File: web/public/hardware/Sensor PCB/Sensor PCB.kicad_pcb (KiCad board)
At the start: 2 copper layers, 65 x 60 mm, 20 parts, among them J1 Conn_01x08_Pin, J2 Conn_01x08_Pin, J3 Conn_01x06_Pin, J4 Conn_01x06_Pin, U1 DRV5033AJxDBZ, U2 DRV5033AJxDBZ, U3 DRV5033AJxDBZ, U4 DRV5033AJxDBZ, U5 74LS11, U6 74LS11

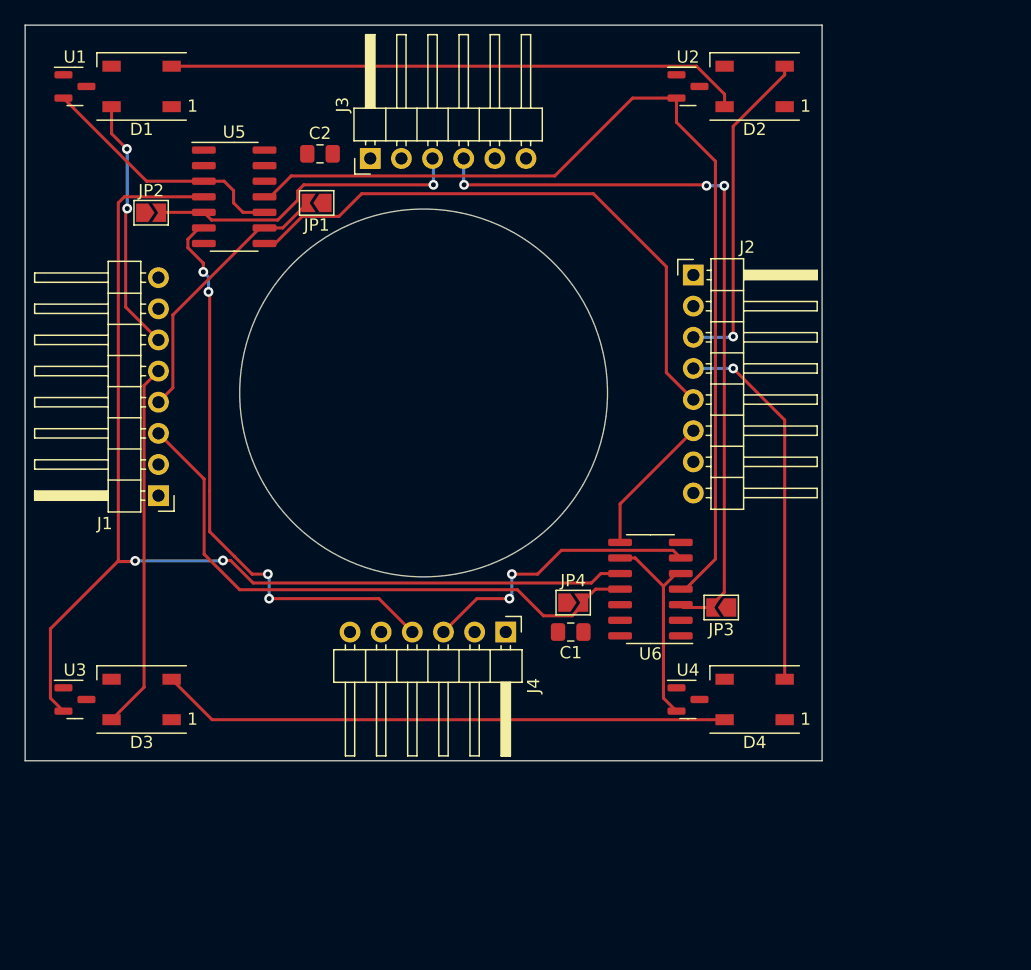
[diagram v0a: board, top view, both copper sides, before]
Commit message: Route PCB power and change sch/PCB page size to US letter
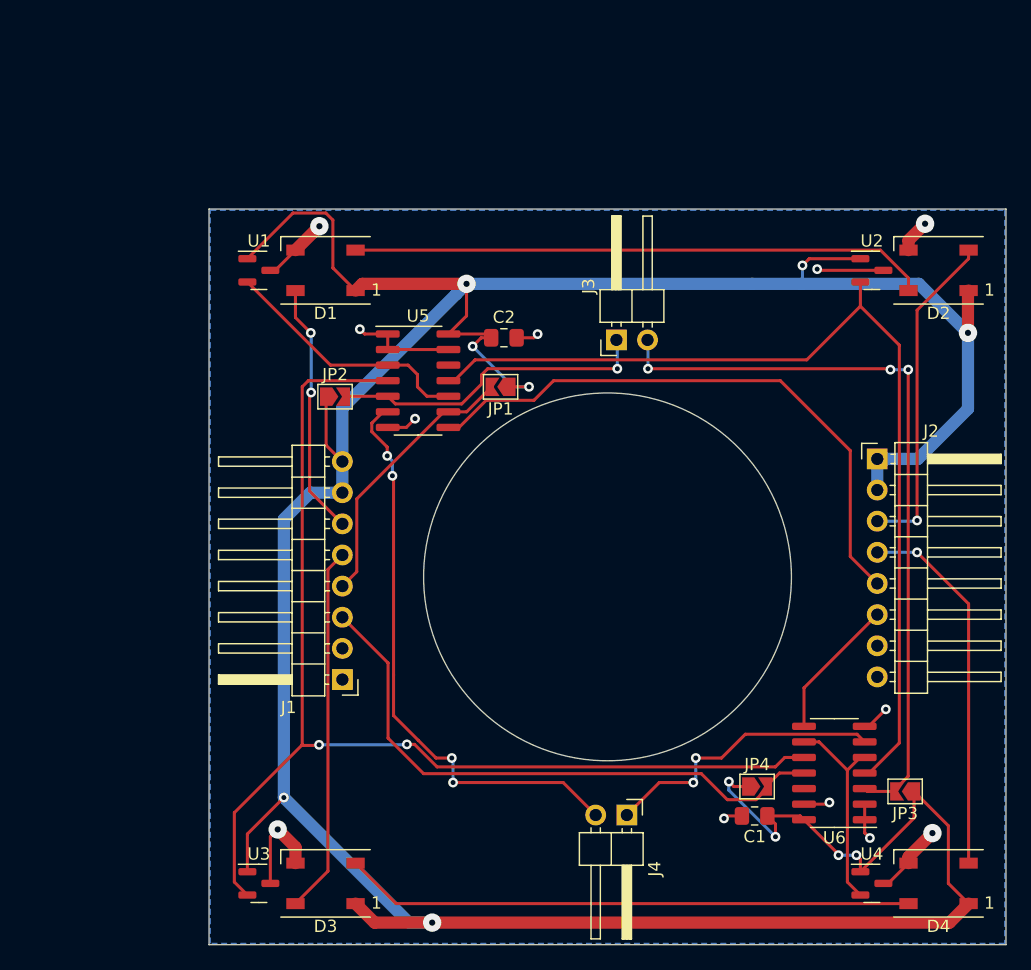
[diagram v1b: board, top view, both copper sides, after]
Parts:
- J3, J4: value Conn_01x06_Pin -> Conn_01x02_Pin; footprint Connector_PinHeader_2.54mm:PinHeader_1x06_P2.54mm_Horizontal -> Connector_PinHeader_2.54mm:PinHeader_1x02_P2.54mm_Horizontal
- moved J3 24.9 mm to (143.2, 70.7)
- moved C2 21.2 mm to (134.1, 70.5)
- moved C1 21.2 mm to (154.5, 109.5)
- moved D1 21.2 mm to (119.5, 65.0)
- moved D2 21.2 mm to (169.5, 65.0)
- moved D3 21.2 mm to (119.5, 115.0)
- moved D4 21.2 mm to (169.5, 115.0)
- moved J1 21.2 mm to (120.9, 98.4)
- moved J2 21.2 mm to (164.5, 80.4)
- moved JP1 21.2 mm to (133.8, 74.5)
- moved JP2 21.2 mm to (120.3, 75.3)
- moved JP3 21.2 mm to (166.8, 107.5)
- moved JP4 21.2 mm to (154.7, 107.1)
- moved U1 21.2 mm to (114.1, 65.0)
- moved U2 21.2 mm to (164.1, 65.0)
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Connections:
- J3 pad 1: +5V -> /COL1_IN
- J3 pad 2: +5V -> /COL2_IN
- J4 pad 1: GND -> /COL2_OUT
- J4 pad 2: GND -> /COL1_OUT
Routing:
- net +5V: track 0.00 -> 282.2 mm, vias 0 -> 11
- net GND: track 0.00 -> 49.6 mm, vias 0 -> 12
- net Net-(U2-OUT): track 79.7 -> 78.9 mm
- added copper zone on B.Cu, net GND

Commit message: Update production files
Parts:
- added H1: MountingHole, MountingHole:MountingHole_2.7mm_M2.5, F.Cu at (130.0, 112.1)
- added H2: MountingHole, MountingHole:MountingHole_2.7mm_M2.5, F.Cu at (113.9, 73.1)
- added H3: MountingHole, MountingHole:MountingHole_2.7mm_M2.5, F.Cu at (159.6, 77.2)
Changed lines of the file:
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@@
   (net 21 "unconnected-(U5-Pad12)")
   (net 22 "unconnected-(U6-Pad12)")
+  (footprint "MountingHole:MountingHole_2.7mm_M2.5" (layer "F.Cu")
+    (at 159.6 77.2)
+    (descr "Mounting Hole 2.7mm, no annular, M2.5")
+    (tags "mounting hole 2.7mm no annular m2.5")
+    (property "Sheetfile" "Sensor PCB.kicad_sch")
+    (property "Sheetname" "")
+    (property "ki_description" "Mounting Hole without connection")
+    (property "ki_keywords" "mounting hole")
+    (attr exclude_from_pos_files)
+    (fp_text reference "H3" (at 0 -3.7) (layer "F.SilkS")
+        (effects (font (size 1 1) (thickness 0.15)))
+    )
+    (fp_text value "MountingHole" (at 0 3.7) (layer "F.Fab")
+        (effects (font (size 1 1) (thickness 0.15)))
+    )
+    (fp_text user "${REFERENCE}" (at 0 0) (layer "F.Fab")
+        (effects (font (size 1 1) (thickness 0.15)))
+    )
+    (fp_circle (center 0 0) (end 2.7 0)
+      (stroke (width 0.15) (type solid)) (fill none) (layer "Cmts.User"))
+    (fp_circle (center 0 0) (end 2.95 0)
+      (stroke (width 0.05) (type solid)) (fill none) (layer "F.CrtYd"))
+    (pad "" np_thru_hole circle (at 0 0) (size 2.7 2.7) (drill 2.7) (layers "*.Cu" "*.Mask"))
+  )
+  (footprint "MountingHole:MountingHole_2.7mm_M2.5" (layer "F.Cu")
+    (at 113.9 73.1)
+    (descr "Mounting Hole 2.7mm, no annular, M2.5")
+    (tags "mounting hole 2.7mm no annular m2.5")
+    (property "Sheetfile" "Sensor PCB.kicad_sch")
+    (property "Sheetname" "")
+    (property "ki_description" "Mounting Hole without connection")
+    (property "ki_keywords" "mounting hole")
+    (attr exclude_from_pos_files)
+    (fp_text reference "H2" (at 0 -3.7) (layer "F.SilkS")
+        (effects (font (size 1 1) (thickness 0.15)))
+    )
+    (fp_text value "MountingHole" (at 0 3.7) (layer "F.Fab")
+        (effects (font (size 1 1) (thickness 0.15)))
+    )
+    (fp_text user "${REFERENCE}" (at 0 0) (layer "F.Fab")
+        (effects (font (size 1 1) (thickness 0.15)))
+    )
+    (fp_circle (center 0 0) (end 2.7 0)
+      (stroke (width 0.15) (type solid)) (fill none) (layer "Cmts.User"))
+    (fp_circle (center 0 0) (end 2.95 0)
+      (stroke (width 0.05) (type solid)) (fill none) (layer "F.CrtYd"))
+    (pad "" np_thru_hole circle (at 0 0) (size 2.7 2.7) (drill 2.7) (layers "*.Cu" "*.Mask"))
+  )
   (footprint "LED_SMD:LED_WS2812B_PLCC4_5.0x5.0mm_P3.2mm" (layer "F.Cu")
     (at 169.5 115 180)
@@
     (fp_line (start 1 0.625) (end -1 0.625)
       (stroke (width 0.1) (type solid)) (layer "F.Fab"))
-    (pad "1" smd roundrect (at -1.0375 0) (size 1.175 1.45) (layers "F.Cu" "F.Paste" "F.Mask") (roundrect_rratio 0.212766)
+    (pad "1" smd roundrect (at -1.0375 0) (size 1.175 1.45) (layers "F.Cu" "F.Paste" "F.Mask") (roundrect_rratio 0.2127659574)
       (net 1 "+5V") (pintype "passive"))
-    (pad "2" smd roundrect (at 1.0375 0) (size 1.175 1.45) (layers "F.Cu" "F.Paste" "F.Mask") (roundrect_rratio 0.212766)
+    (pad "2" smd roundrect (at 1.0375 0) (size 1.175 1.45) (layers "F.Cu" "F.Paste" "F.Mask") (roundrect_rratio 0.2127659574)
       (net 2 "GND") (pintype "passive"))
     (model "${KICAD6_3DMODEL_DIR}/Capacitor_SMD.3dshapes/C_0805_2012Metric.wrl"
@@
     )
   )
+  (footprint "MountingHole:MountingHole_2.7mm_M2.5" (layer "F.Cu")
+    (at 130 112.1)
+    (descr "Mounting Hole 2.7mm, no annular, M2.5")
+    (tags "mounting hole 2.7mm no annular m2.5")
+    (property "Sheetfile" "Sensor PCB.kicad_sch")
+    (property "Sheetname" "")
+    (property "ki_description" "Mounting Hole without connection")
+    (property "ki_keywords" "mounting hole")
+    (attr exclude_from_pos_files)
+    (fp_text reference "H1" (at 0 -3.7) (layer "F.SilkS")
+        (effects (font (size 1 1) (thickness 0.15)))
+    )
+    (fp_text value "MountingHole" (at 0 3.7) (layer "F.Fab")
+        (effects (font (size 1 1) (thickness 0.15)))
+    )
+    (fp_text user "${REFERENCE}" (at 0 0) (layer "F.Fab")
+        (effects (font (size 1 1) (thickness 0.15)))
+    )
+    (fp_circle (center 0 0) (end 2.7 0)
+      (stroke (width 0.15) (type solid)) (fill none) (layer "Cmts.User"))
+    (fp_circle (center 0 0) (end 2.95 0)
+      (stroke (width 0.05) (type solid)) (fill none) (layer "F.CrtYd"))
+    (pad "" np_thru_hole circle (at 0 0) (size 2.7 2.7) (drill 2.7) (layers "*.Cu" "*.Mask"))
+  )
   (footprint "Jumper:SolderJumper-2_P1.3mm_Open_TrianglePad1.0x1.5mm" (layer "F.Cu")
     (at 154.7 107.1)
@@
     (fp_line (start 1 0.625) (end -1 0.625)
       (stroke (width 0.1) (type solid)) (layer "F.Fab"))
-    (pad "1" smd roundrect (at -1.0375 0 180) (size 1.175 1.45) (layers "F.Cu" "F.Paste" "F.Mask") (roundrect_rratio 0.212766)
+    (pad "1" smd roundrect (at -1.0375 0 180) (size 1.175 1.45) (layers "F.Cu" "F.Paste" "F.Mask") (roundrect_rratio 0.2127659574)
       (net 1 "+5V") (pintype "passive"))
-    (pad "2" smd roundrect (at 1.0375 0 180) (size 1.175 1.45) (layers "F.Cu" "F.Paste" "F.Mask") (roundrect_rratio 0.212766)
+    (pad "2" smd roundrect (at 1.0375 0 180) (size 1.175 1.45) (layers "F.Cu" "F.Paste" "F.Mask") (roundrect_rratio 0.2127659574)
       (net 2 "GND") (pintype "passive"))
     (model "${KICAD6_3DMODEL_DIR}/Capacitor_SMD.3dshapes/C_0805_2012Metric.wrl"
@@
   (segment (start 154.60962 108.175) (end 155.425 107.35962) (width 0.25) (layer "F.Cu") (net 10))
   (segment (start 127.5 106.05) (end 150.15 106.05) (width 0.25) (layer "F.Cu") (net 10))
-  (segment (start 156.6 74) (end 162.3 79.7) (width 0.25) (layer "F.Cu") (net 11))
-  (segment (start 138.1 74) (end 156.6 74) (width 0.25) (layer "F.Cu") (net 11))
   (segment (start 129.525 77.81) (end 130.39 77.81) (width 0.25) (layer "F.Cu") (net 11))
-  (segment (start 162.3 79.7) (end 162.3 88.34) (width 0.25) (layer "F.Cu") (net 11))
+  (segment (start 132.6 75.6) (end 136.5 75.6) (width 0.25) (layer "F.Cu") (net 11))
+  (segment (start 155 79.3) (end 156.9 81.2) (width 0.25) (layer "F.Cu") (net 11))
+  (segment (start 161.1 81.2) (end 162.3 82.4) (width 0.25) (layer "F.Cu") (net 11))
+  (segment (start 138.1 74) (end 152.3 74) (width 0.25) (layer "F.Cu") (net 11))
+  (segment (start 155 76.7) (end 155 79.3) (width 0.25) (layer "F.Cu") (net 11))
+  (segment (start 130.39 77.81) (end 132.6 75.6) (width 0.25) (layer "F.Cu") (net 11))
+  (segment (start 162.3 82.4) (end 162.3 88.34) (width 0.25) (layer "F.Cu") (net 11))
+  (segment (start 156.9 81.2) (end 161.1 81.2) (width 0.25) (layer "F.Cu") (net 11))
   (segment (start 136.5 75.6) (end 138.1 74) (width 0.25) (layer "F.Cu") (net 11))
-  (segment (start 130.39 77.81) (end 132.6 75.6) (width 0.25) (layer "F.Cu") (net 11))
-  (segment (start 132.6 75.6) (end 136.5 75.6) (width 0.25) (layer "F.Cu") (net 11))
   (segment (start 162.3 88.34) (end 164.5 90.54) (width 0.25) (layer "F.Cu") (net 11))
+  (segment (start 152.3 74) (end 155 76.7) (width 0.25) (layer "F.Cu") (net 11))
   (segment (start 158.525 102.19) (end 158.525 99.055) (width 0.25) (layer "F.Cu") (net 12))
   (segment (start 158.525 99.055) (end 164.5 93.08) (width 0.25) (layer "F.Cu") (net 12))

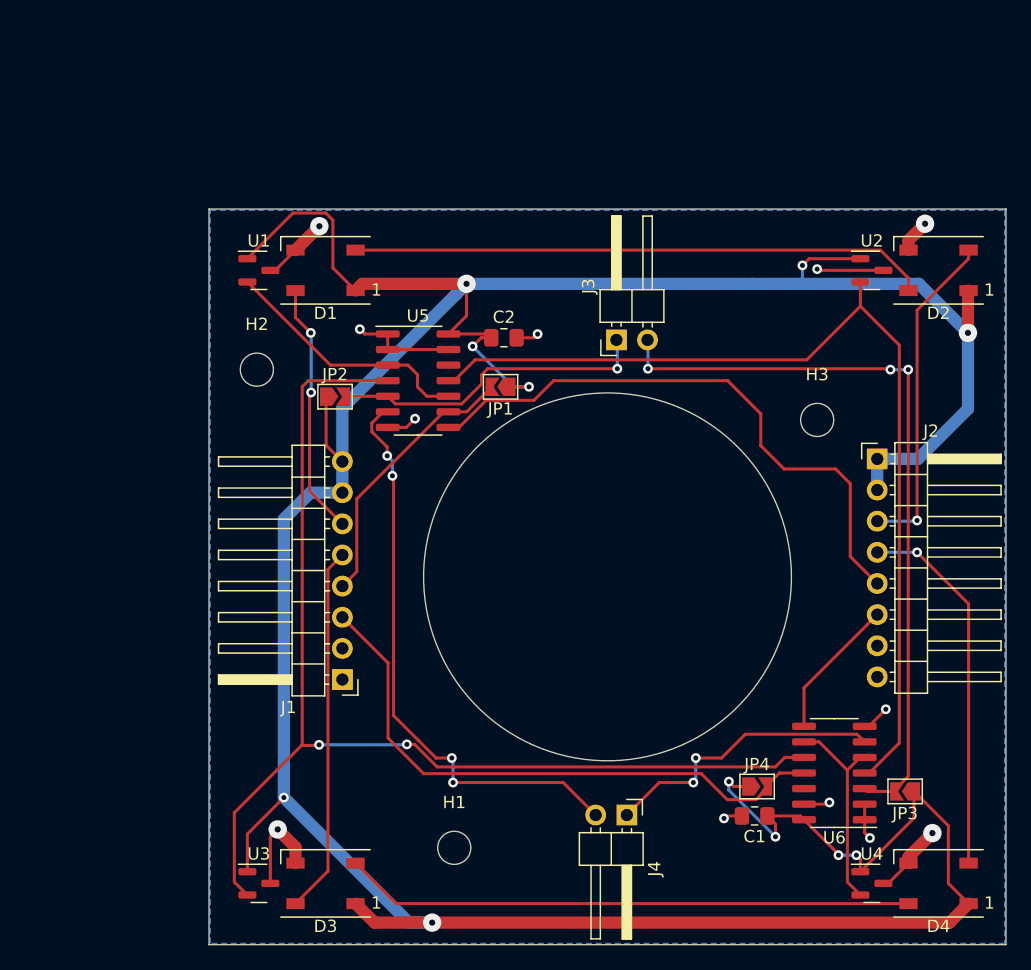
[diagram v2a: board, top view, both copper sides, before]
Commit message: Add pullup resistor to hall effect sensor for open-drain sensors
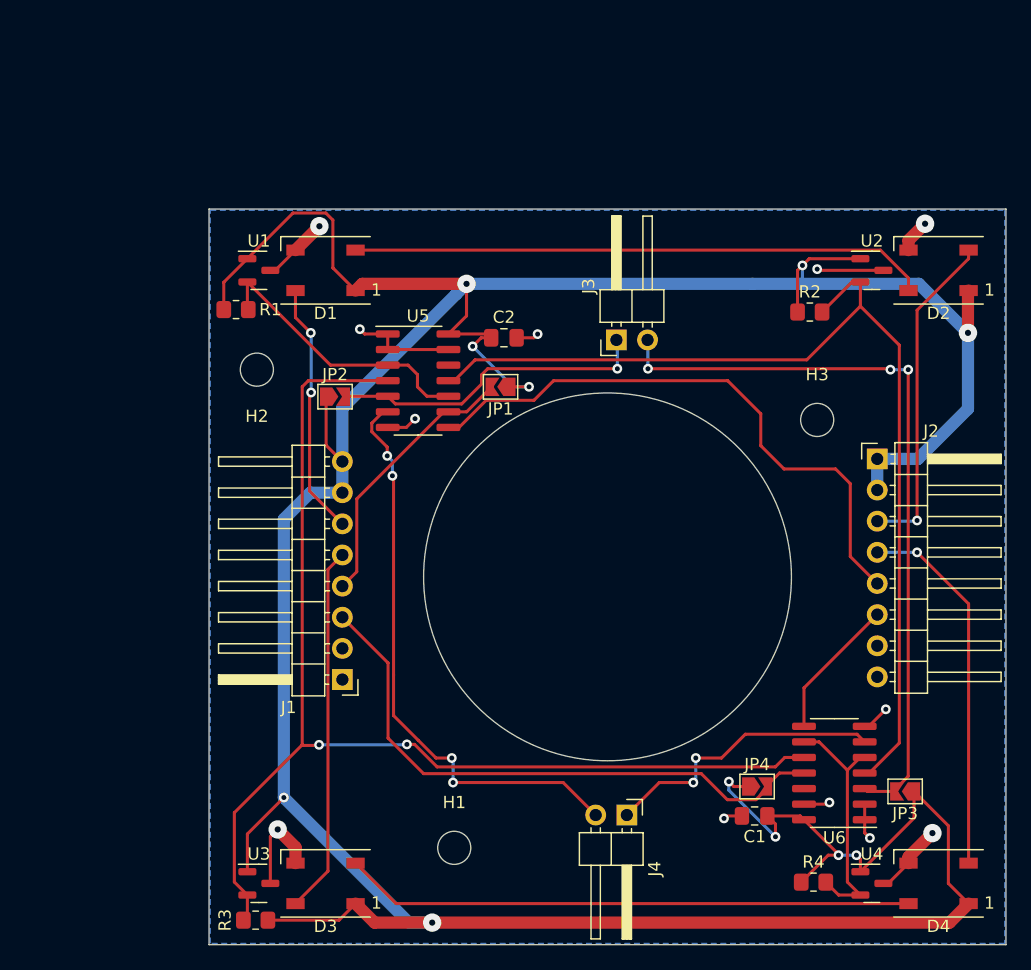
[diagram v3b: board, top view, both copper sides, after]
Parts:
- added R1: 10K, Resistor_SMD:R_0805_2012Metric_Pad1.20x1.40mm_HandSolder, F.Cu at (112.2, 68.2)
- added R2: 10K, Resistor_SMD:R_0805_2012Metric_Pad1.20x1.40mm_HandSolder, F.Cu at (159.0, 68.4)
- added R3: 10K, Resistor_SMD:R_0805_2012Metric_Pad1.20x1.40mm_HandSolder, F.Cu at (113.8, 118.0)
- added R4: 10K, Resistor_SMD:R_0805_2012Metric_Pad1.20x1.40mm_HandSolder, F.Cu at (159.3, 114.9)
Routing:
- net +5V: track 282.2 -> 302.8 mm
- net Net-(U2-OUT): track 78.9 -> 83.0 mm
- net Net-(U4-OUT): track 17.0 -> 20.2 mm
- net Net-(U1-OUT): track 20.8 -> 23.1 mm
- net Net-(U3-OUT): track 93.4 -> 95.6 mm

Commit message: Fix routing to fit hall effect decoupling capacitors
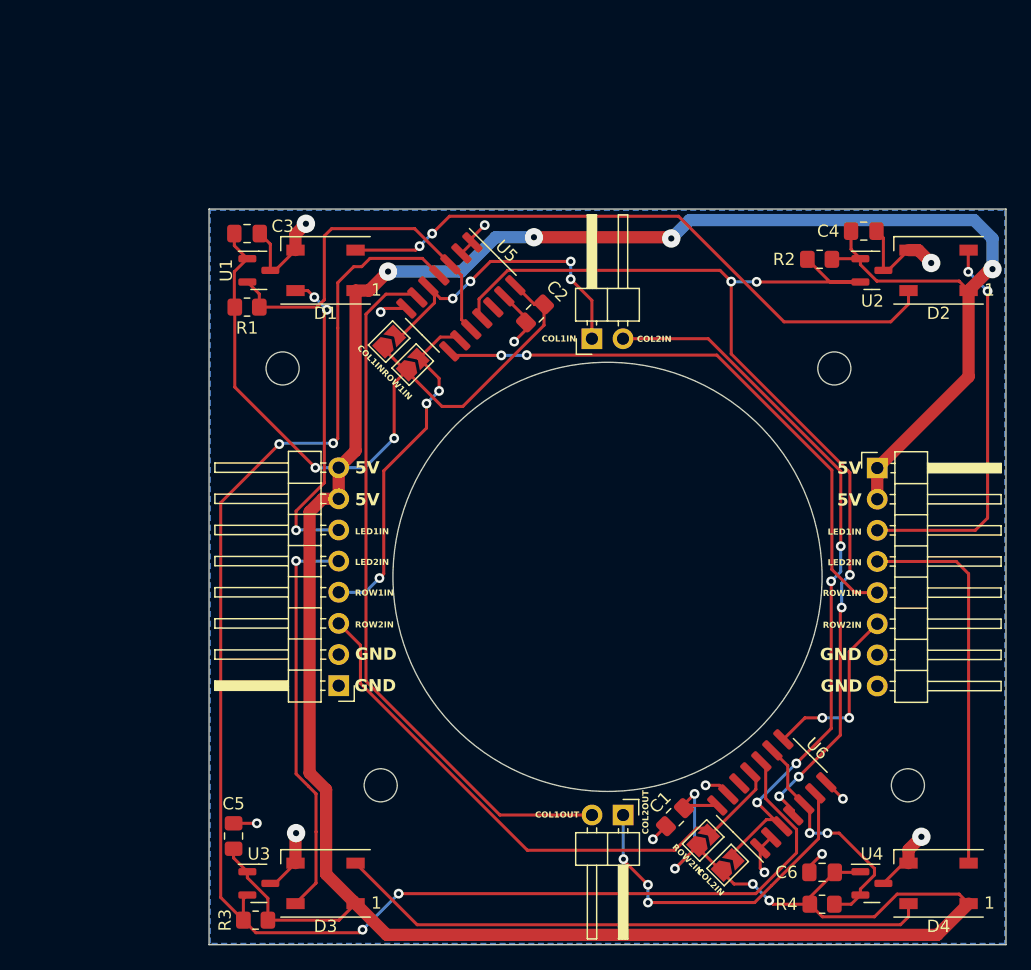
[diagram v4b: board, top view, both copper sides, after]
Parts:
- added C3: 0.1uF, Capacitor_SMD:C_0805_2012Metric_Pad1.18x1.45mm_HandSolder, F.Cu at (113.1, 62.0)
- added C4: 0.1uF, Capacitor_SMD:C_0805_2012Metric_Pad1.18x1.45mm_HandSolder, F.Cu at (163.4, 61.8)
- added C5: 0.1uF, Capacitor_SMD:C_0805_2012Metric_Pad1.18x1.45mm_HandSolder, F.Cu at (112.0, 111.1)
- added C6: 0.1uF, Capacitor_SMD:C_0805_2012Metric_Pad1.18x1.45mm_HandSolder, F.Cu at (160.0, 114.1)
- added H4: MountingHole, MountingHole:MountingHole_2.7mm_M2.5, F.Cu at (167.0, 107.0)
- moved H1 41.5 mm to (116.0, 73.0)
- moved H2 35.4 mm to (124.0, 107.0)
- moved JP3 15.7 mm to (152.3, 113.5), turned to 45 degrees
- moved U5 7.68 mm to (130.5, 67.2), turned to -45 degrees
- moved JP1 7.39 mm to (126.6, 72.7), turned to 45 degrees
- moved C1 6.50 mm to (148.0, 109.6), turned to -135 degrees
- moved JP2 6.29 mm to (124.7, 70.8), turned to 45 degrees
- moved JP4 6.22 mm to (150.3, 111.5), turned to 45 degrees
- moved U6 5.38 mm to (155.9, 107.7), turned to 135 degrees
- moved H3 4.43 mm to (161.0, 73.0)
- moved R2 4.37 mm to (159.8, 64.1), turned to 180 degrees
- moved C2 3.22 mm to (136.6, 68.5), turned to -135 degrees
- moved J3 2.00 mm to (141.2, 70.6)
- moved R4 1.93 mm to (160.0, 116.7)
- moved R1 0.92 mm to (113.1, 68.0)
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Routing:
- net Net-(U3-OUT): track 95.6 -> 128.0 mm, vias 2 -> 4
- net +5V: track 302.8 -> 319.8 mm, vias 11 -> 10
- net /COL1_OUT: track 47.2 -> 57.9 mm, vias 4 -> 0
- net Net-(U1-OUT): track 23.1 -> 30.9 mm
- net Net-(U2-OUT): track 83.0 -> 89.7 mm, vias 0 -> 6
- net /ROW1_IN: track 22.4 -> 28.6 mm, vias 0 -> 3
- net /LED1_IN: track 20.7 -> 26.0 mm, vias 2 -> 3
- net /LED1_OUT: track 27.1 -> 31.9 mm, vias 1 -> 2
- net Net-(D1-DOUT): track 47.1 -> 51.5 mm, vias 0 -> 2
- net /COL2_OUT: track 23.4 -> 27.9 mm, vias 2 -> 3
- net /ROW2_OUT: track 11.6 -> 14.7 mm, vias 0 -> 2
- net /LED2_IN: track 30.0 -> 32.8 mm, vias 0 -> 1
- net Net-(D3-DOUT): track 46.5 -> 48.5 mm
- net /LED2_OUT: track 30.3 -> 31.5 mm, vias 1 -> 0
- net GND: track 49.6 -> 50.5 mm, vias 12 -> 13
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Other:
- outline, holes or cut-outs redrawn
- board text added: "5V"
- board text added: "COL1IN"
- board text added: "COL1OUT"
- board text added: "COL2IN"
- board text added: "COL2OUT"
- board text added: "GND"
- board text added: "LED1IN"
- board text added: "LED2IN"
- board text added: "ROW1IN"
- board text added: "ROW2IN"
